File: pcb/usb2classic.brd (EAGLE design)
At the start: 99.8 x 80 mm, 28 parts, among them IC2 74HC595N, IC3 74HC595N, IC6 EPM7064S44, IC7 74HC153N, IC8 74HC153N, X2 GLX-S-88M, X5 2510-, X6 GLX-S-88M

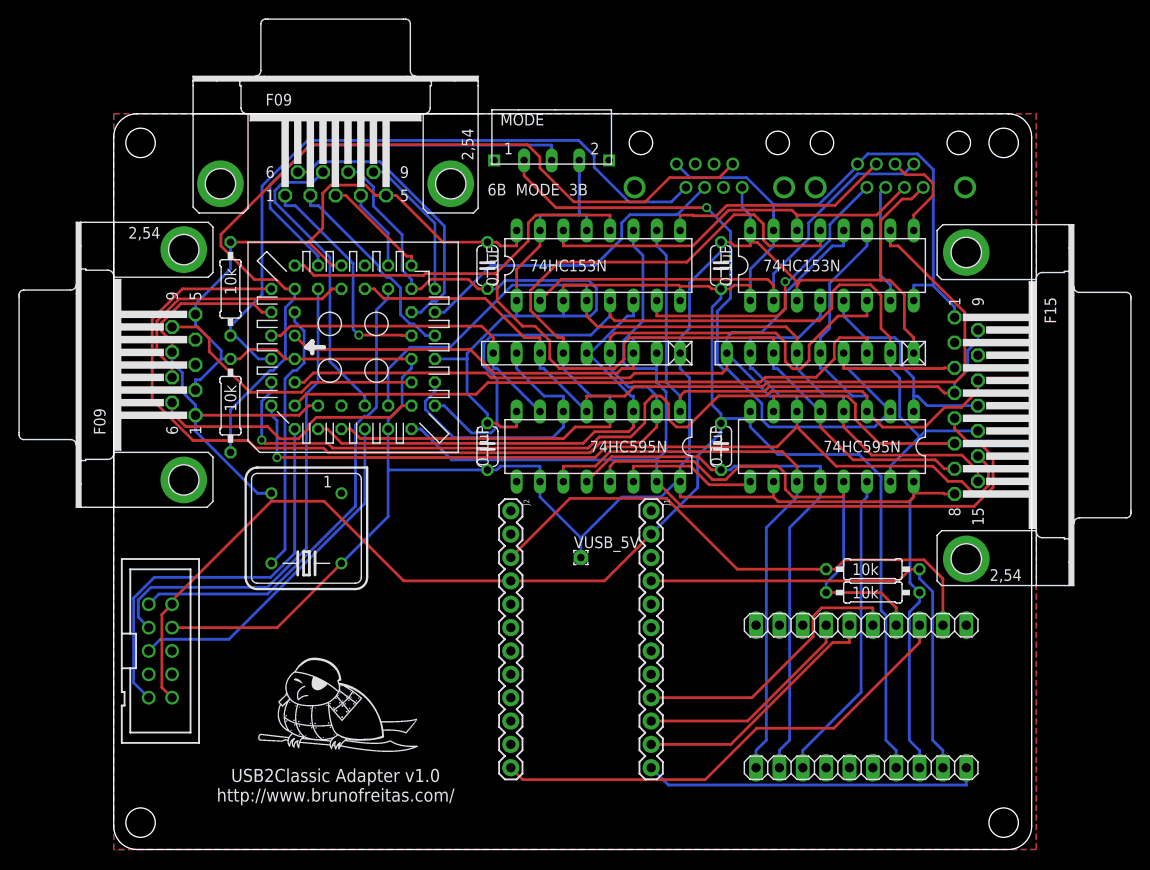
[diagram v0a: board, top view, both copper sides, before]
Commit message: Added pull-down resistor to NES/SNES data line. This is an attempt to fix issue #1
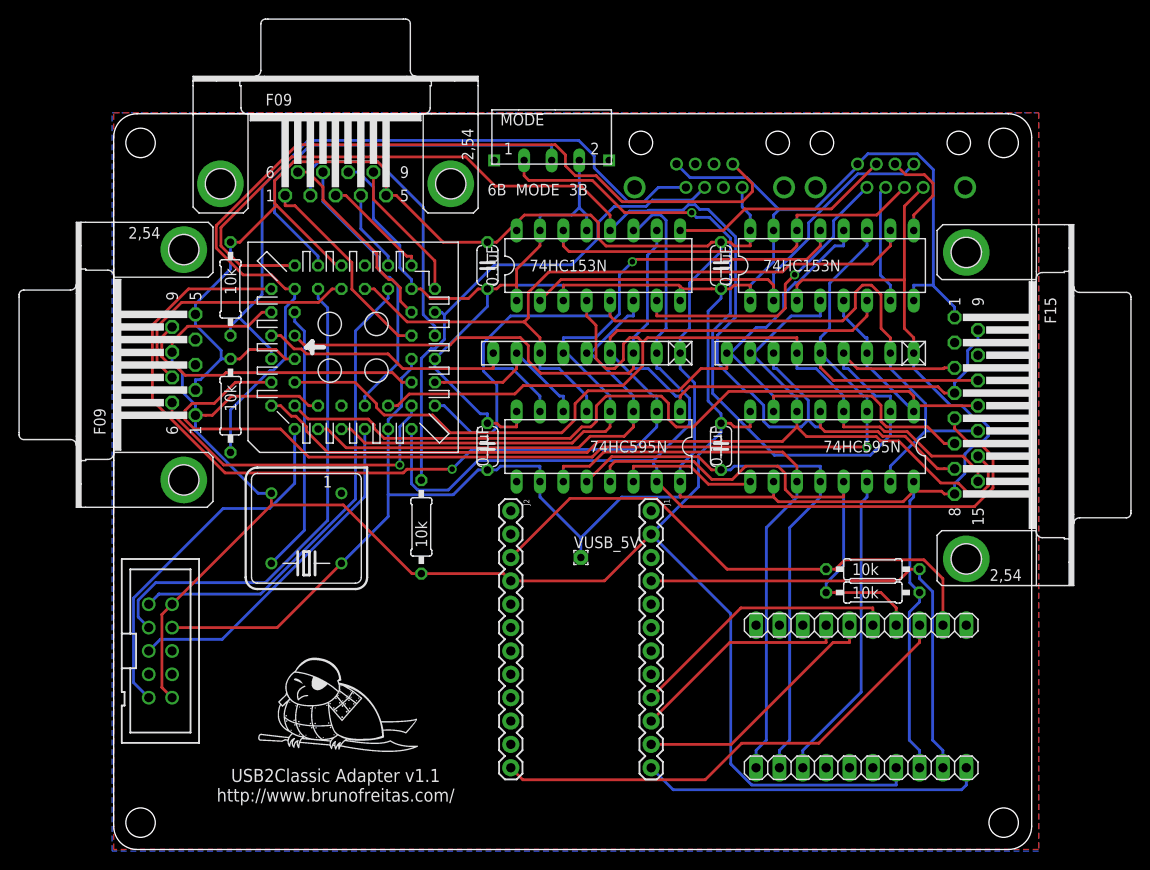
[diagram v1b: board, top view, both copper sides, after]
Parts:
- added R5: 10k, resistor:0207/10
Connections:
- net GND: now also R5.1
- net INPUT_DATA: now also R5.2
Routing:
- net VCC: track 322.9 -> 359.6 mm
- net O5: track 108.5 -> 136.1 mm
- net INPUT_DATA: track 36.0 -> 55.5 mm
- net GND: track 400.7 -> 384.1 mm
- net O13: track 94.8 -> 79.1 mm
- net O3: track 123.0 -> 135.2 mm
- net O14: track 31.5 -> 19.9 mm
- net O12: track 89.2 -> 79.0 mm, vias 0 -> 1
- net GEN_P6: track 31.0 -> 21.2 mm
- net GEN_P2: track 22.4 -> 32.0 mm
- net O8: track 110.9 -> 119.1 mm
- net O4: track 87.3 -> 94.6 mm
- net INPUT_LATCH: track 96.8 -> 103.2 mm
- net O1: track 94.2 -> 100.4 mm
- net O2: track 87.4 -> 92.8 mm
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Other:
- board text added: "USB2Classic Adapter v1.1 http://www.brunofreitas.com/"
- board text removed: "USB2Classic Adapter v1.0 http://www.brunofreitas.com/"

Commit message: Removed not used signal traces from the CPLD
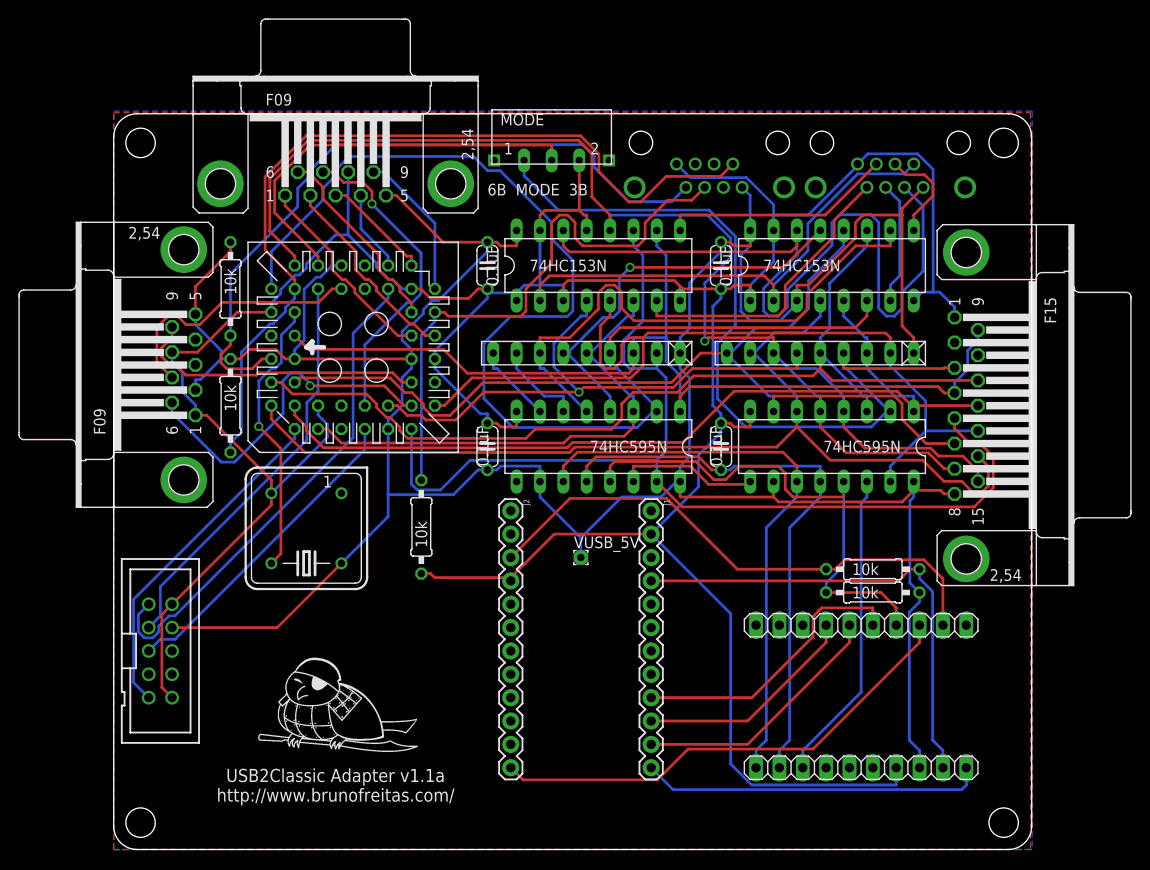
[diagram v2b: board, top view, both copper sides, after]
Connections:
- net O12: no longer IC6.11
- net O13: no longer IC6.34
- net O14: no longer IC6.20
- net O15: no longer IC6.44
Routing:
- net SAT_S0: track 43.9 -> 87.3 mm
- net O12: track 79.0 -> 44.4 mm
- net O15: track 37.0 -> 8.69 mm
- net O3: track 135.2 -> 110.3 mm, vias 1 -> 0
- net VCC: track 359.6 -> 340.5 mm
- net O13: track 79.1 -> 60.5 mm
- net O5: track 136.1 -> 121.4 mm, vias 0 -> 1
- net GND: track 384.1 -> 371.1 mm
- net INPUT_LATCH: track 103.2 -> 92.9 mm
- net O14: track 19.9 -> 9.67 mm
- net GEN_P2: track 32.0 -> 21.9 mm
- net TDO: track 53.3 -> 44.5 mm
- net INPUT_DATA: track 55.5 -> 63.0 mm
- net O10: track 125.6 -> 132.8 mm, vias 1 -> 0
- net O0: track 98.7 -> 94.1 mm
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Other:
- board text added: "USB2Classic Adapter v1.1a http://www.brunofreitas.com/"
- board text removed: "USB2Classic Adapter v1.1 http://www.brunofreitas.com/"
